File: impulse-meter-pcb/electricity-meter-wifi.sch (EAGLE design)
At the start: 13 parts, among them U2 MCP1316MT-29ME/OT

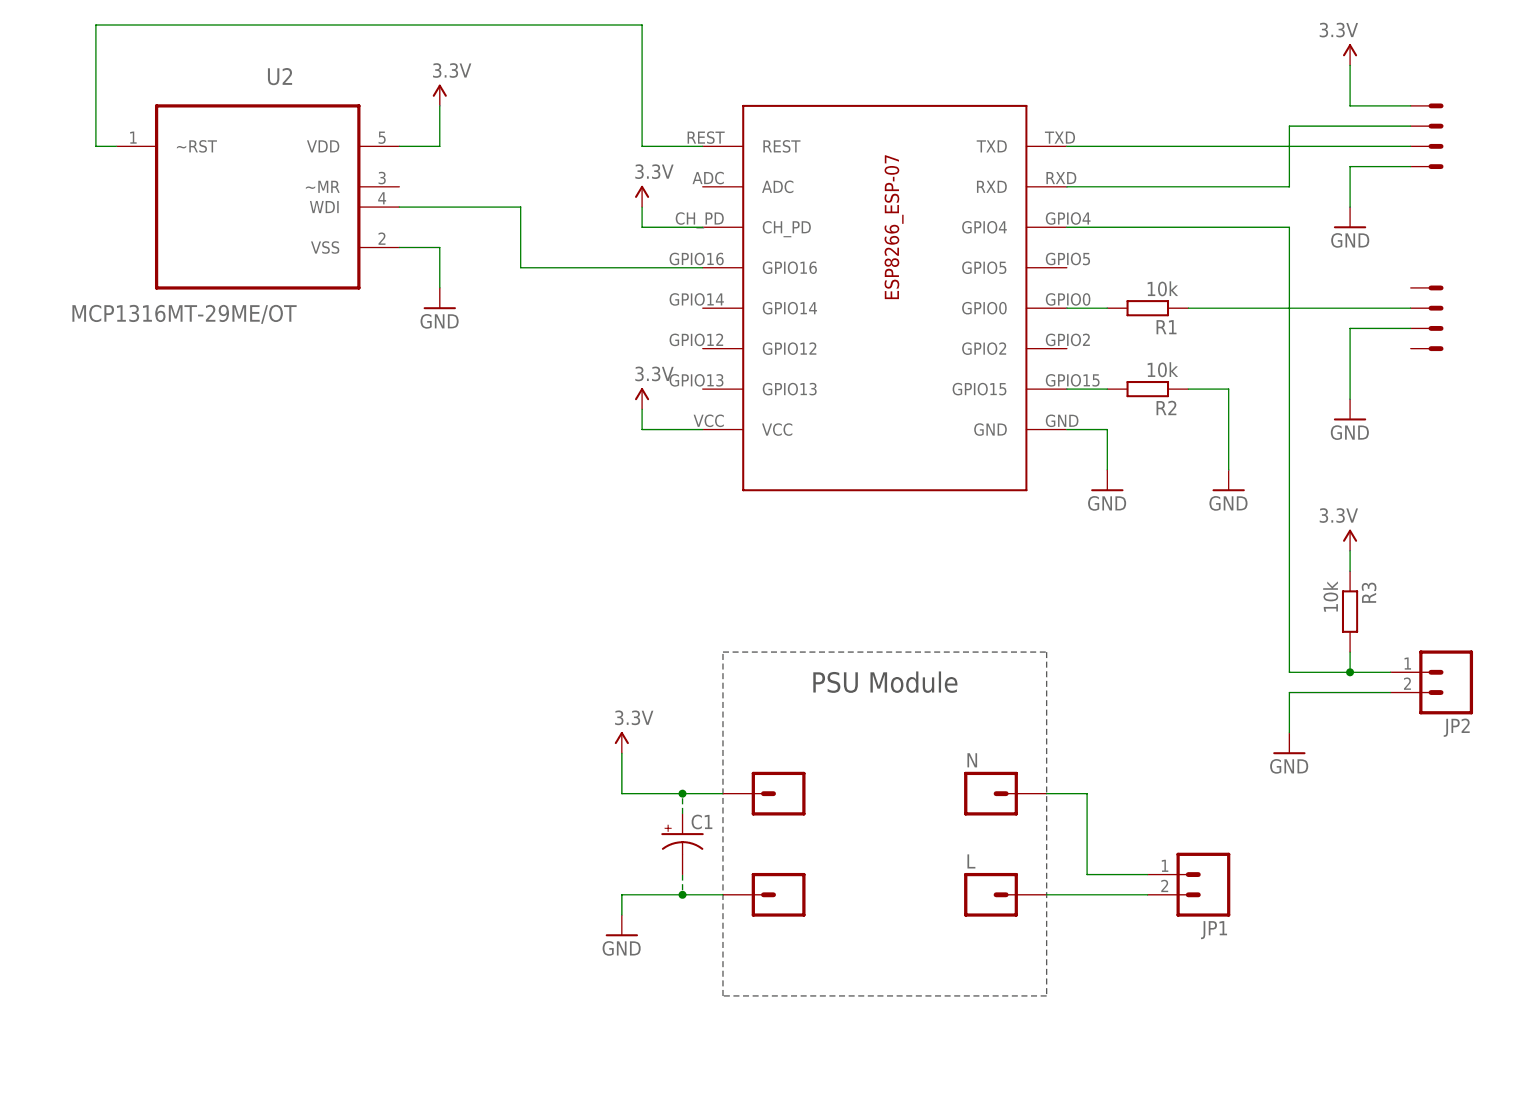
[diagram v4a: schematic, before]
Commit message: PCB: v.1.4.1 Added FeRAM
+ docs
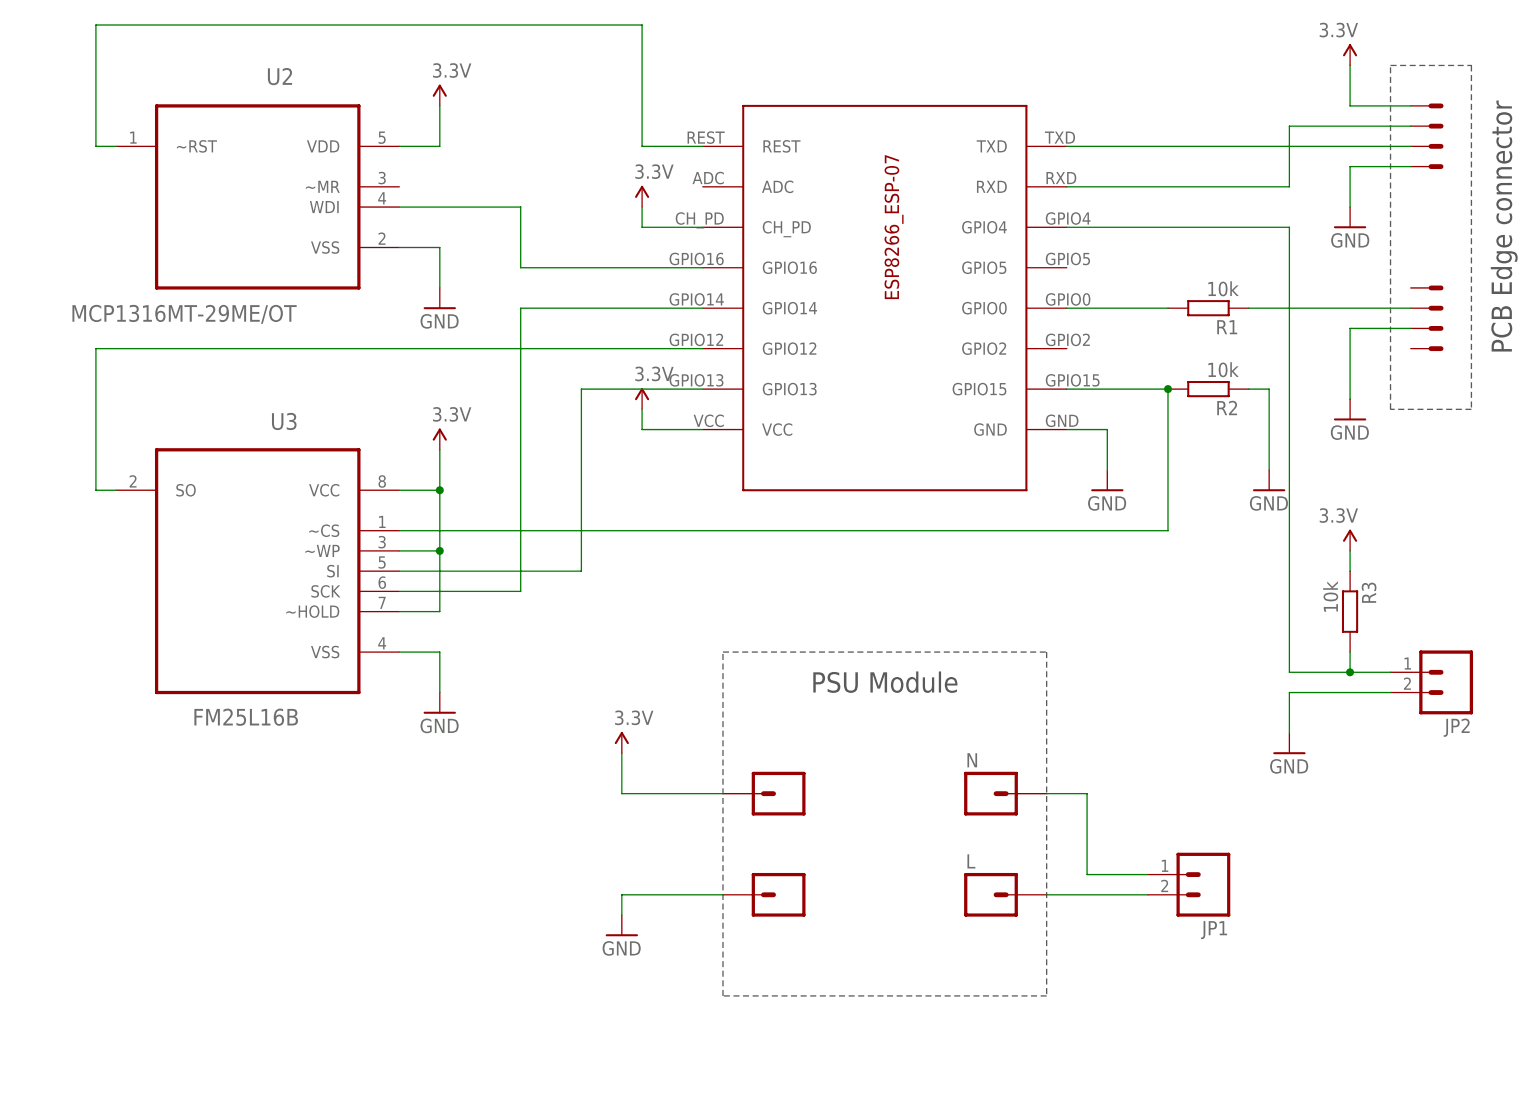
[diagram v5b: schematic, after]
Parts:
- removed C1: (no value), SparkFun-Capacitors:CAP_POLD
- added U3: FM25L16B, Microchip_By_element14_Batch_1:25AA020A-I/SN
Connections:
- new net N$10: ESP8266_ESP-07.GPIO12, U3.SO
- new net N$12: ESP8266_ESP-07.GPIO13, U3.SI
- new net N$13: ESP8266_ESP-07.GPIO14, U3.SCK
- net 3.3V: now also U3.VCC, U3.~HOLD, U3.~WP; no longer C1.+
- net GND: now also U3.VSS; no longer C1.-
- net N$7: now also U3.~CS
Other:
- note added: "PCB Edge connector"
- moved on the sheet: R1, R2
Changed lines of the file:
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@@
 <part name="JP1" library="SparkFun (old)" deviceset="M02" device="PTH3_5MM"/>
 <part name="JP2" library="SparkFun (old)" deviceset="M02" device="PTH3_5MM"/>
-<part name="C1" library="SparkFun-Capacitors" deviceset="CAP_POL" device="D"/>
 <part name="U$1" library="con-pcb-slot" deviceset="CON-PCB-SLOT-0.05" device="MINIMAL"/>
 <part name="GND2" library="SparkFun-Aesthetics" deviceset="GND" device=""/>
@@
 <part name="SUPPLY5" library="SparkFun-Aesthetics" deviceset="3.3V" device=""/>
 <part name="GND6" library="SparkFun-Aesthetics" deviceset="GND" device=""/>
+<part name="U3" library="Microchip_By_element14_Batch_1" deviceset="25AA020A-I/SN" device="" value="FM25L16B"/>
+<part name="GND7" library="SparkFun-Aesthetics" deviceset="GND" device=""/>
+<part name="SUPPLY6" library="SparkFun-Aesthetics" deviceset="3.3V" device=""/>
 </parts>
 <sheets>
@@
 <wire x1="129.54" y1="-27.94" x2="88.9" y2="-27.94" width="0.1524" layer="97" style="longdash"/>
 <text x="109.22" y="10.16" size="2.54" layer="97" align="bottom-center">PSU Module</text>
+<wire x1="172.72" y1="45.72" x2="172.72" y2="88.9" width="0.1524" layer="97" style="longdash"/>
+<wire x1="172.72" y1="88.9" x2="182.88" y2="88.9" width="0.1524" layer="97" style="longdash"/>
+<wire x1="182.88" y1="88.9" x2="182.88" y2="45.72" width="0.1524" layer="97" style="longdash"/>
+<wire x1="182.88" y1="45.72" x2="172.72" y2="45.72" width="0.1524" layer="97" style="longdash"/>
+<text x="187.96" y="68.58" size="2.54" layer="97" rot="R90" align="bottom-center">PCB Edge connector</text>
 </plain>
 <instances>
@@
 <instance part="SUPPLY4" gate="G$1" x="167.64" y="88.9" rot="MR0"/>
 <instance part="GND5" gate="1" x="167.64" y="44.45"/>
-<instance part="R1" gate="G$1" x="142.24" y="58.42" rot="R180"/>
+<instance part="R1" gate="G$1" x="149.86" y="58.42" rot="R180"/>
 <instance part="ESP8266_ESP-07" gate="G$1" x="106.68" y="53.34" smashed="yes">
 <attribute name="NAME" x="109.22" y="68.58" size="1.778" layer="94" rot="R270" align="bottom-center"/>
@@
 <instance part="JP1" gate="G$1" x="149.86" y="-12.7" rot="R180"/>
 <instance part="JP2" gate="G$1" x="180.34" y="12.7" rot="R180"/>
-<instance part="C1" gate="G$1" x="83.82" y="-7.62"/>
 <instance part="U$1" gate="G$1" x="175.26" y="76.2" smashed="yes" rot="MR180"/>
 <instance part="U$1" gate="G$2" x="175.26" y="78.74" smashed="yes" rot="MR180"/>
@@
 <instance part="R3" gate="G$1" x="167.64" y="20.32" rot="R270"/>
 <instance part="SUPPLY3" gate="G$1" x="167.64" y="27.94" rot="MR0"/>
-<instance part="R2" gate="G$1" x="142.24" y="48.26" rot="R180"/>
-<instance part="GND3" gate="1" x="152.4" y="35.56"/>
+<instance part="R2" gate="G$1" x="149.86" y="48.26" rot="R180"/>
+<instance part="GND3" gate="1" x="157.48" y="35.56"/>
 <instance part="U2" gate="A" x="30.48" y="76.2" rot="MR0"/>
 <instance part="SUPPLY5" gate="G$1" x="53.34" y="83.82"/>
 <instance part="GND6" gate="1" x="53.34" y="58.42"/>
+<instance part="U3" gate="A" x="30.48" y="27.94" rot="MR0"/>
+<instance part="GND7" gate="1" x="53.34" y="7.62"/>
+<instance part="SUPPLY6" gate="G$1" x="53.34" y="40.64"/>
 </instances>
 <busses>
@@
 <pinref part="GND" gate="G$1" pin="1"/>
 <pinref part="GND1" gate="1" pin="GND"/>
-<wire x1="88.9" y1="-15.24" x2="83.82" y2="-15.24" width="0.1524" layer="91"/>
-<wire x1="83.82" y1="-15.24" x2="76.2" y2="-15.24" width="0.1524" layer="91"/>
+<wire x1="88.9" y1="-15.24" x2="76.2" y2="-15.24" width="0.1524" layer="91"/>
 <wire x1="76.2" y1="-15.24" x2="76.2" y2="-17.78" width="0.1524" layer="91"/>
-<pinref part="C1" gate="G$1" pin="-"/>
-<wire x1="83.82" y1="-12.7" x2="83.82" y2="-15.24" width="0.1524" layer="91" style="longdash"/>
-<junction x="83.82" y="-15.24"/>
 </segment>
 <segment>
@@
 <segment>
 <pinref part="GND3" gate="1" pin="GND"/>
-<wire x1="152.4" y1="38.1" x2="152.4" y2="48.26" width="0.1524" layer="91"/>
+<wire x1="157.48" y1="38.1" x2="157.48" y2="48.26" width="0.1524" layer="91"/>
 <pinref part="R2" gate="G$1" pin="1"/>
-<wire x1="152.4" y1="48.26" x2="147.32" y2="48.26" width="0.1524" layer="91"/>
+<wire x1="157.48" y1="48.26" x2="154.94" y2="48.26" width="0.1524" layer="91"/>
 </segment>
 <segment>
@@
 <wire x1="53.34" y1="66.04" x2="53.34" y2="60.96" width="0.1524" layer="91"/>
 </segment>
+<segment>
+<pinref part="U3" gate="A" pin="VSS"/>
+<pinref part="GND7" gate="1" pin="GND"/>
+<wire x1="48.26" y1="15.24" x2="53.34" y2="15.24" width="0.1524" layer="91"/>
+<wire x1="53.34" y1="15.24" x2="53.34" y2="10.16" width="0.1524" layer="91"/>
+</segment>
 </net>
 <net name="3.3V" class="0">
@@
 <pinref part="3.3V" gate="G$1" pin="1"/>
 <pinref part="SUPPLY1" gate="G$1" pin="3.3V"/>
-<wire x1="88.9" y1="-2.54" x2="83.82" y2="-2.54" width="0.1524" layer="91"/>
-<wire x1="83.82" y1="-2.54" x2="76.2" y2="-2.54" width="0.1524" layer="91"/>
+<wire x1="88.9" y1="-2.54" x2="76.2" y2="-2.54" width="0.1524" layer="91"/>
 <wire x1="76.2" y1="-2.54" x2="76.2" y2="2.54" width="0.1524" layer="91"/>
-<pinref part="C1" gate="G$1" pin="+"/>
-<wire x1="83.82" y1="-5.08" x2="83.82" y2="-2.54" width="0.1524" layer="91" style="longdash"/>
-<junction x="83.82" y="-2.54"/>
 </segment>
 <segment>
@@
 <wire x1="53.34" y1="78.74" x2="53.34" y2="83.82" width="0.1524" layer="91"/>
 </segment>
+<segment>
+<pinref part="U3" gate="A" pin="VCC"/>
+<pinref part="SUPPLY6" gate="G$1" pin="3.3V"/>
+<wire x1="48.26" y1="35.56" x2="53.34" y2="35.56" width="0.1524" layer="91"/>
+<wire x1="53.34" y1="35.56" x2="53.34" y2="40.64" width="0.1524" layer="91"/>
+<pinref part="U3" gate="A" pin="~WP"/>
+<wire x1="48.26" y1="27.94" x2="53.34" y2="27.94" width="0.1524" layer="91"/>
+<wire x1="53.34" y1="27.94" x2="53.34" y2="35.56" width="0.1524" layer="91"/>
+<junction x="53.34" y="35.56"/>
+<pinref part="U3" gate="A" pin="~HOLD"/>
+<wire x1="48.26" y1="20.32" x2="53.34" y2="20.32" width="0.1524" layer="91"/>
+<wire x1="53.34" y1="20.32" x2="53.34" y2="27.94" width="0.1524" layer="91"/>
+<junction x="53.34" y="27.94"/>
+</segment>
 </net>
 <net name="N$11" class="0">
@@
 <pinref part="R1" gate="G$1" pin="1"/>
 <pinref part="U$1" gate="G$6" pin="S"/>
-<wire x1="147.32" y1="58.42" x2="175.26" y2="58.42" width="0.1524" layer="91"/>
+<wire x1="154.94" y1="58.42" x2="175.26" y2="58.42" width="0.1524" layer="91"/>
 </segment>
 </net>
@@
 <pinref part="R1" gate="G$1" pin="2"/>
 <pinref part="ESP8266_ESP-07" gate="G$1" pin="GPIO0"/>
-<wire x1="137.16" y1="58.42" x2="132.08" y2="58.42" width="0.1524" layer="91"/>
+<wire x1="144.78" y1="58.42" x2="132.08" y2="58.42" width="0.1524" layer="91"/>
 </segment>
 </net>
@@
 <pinref part="R2" gate="G$1" pin="2"/>
 <pinref part="ESP8266_ESP-07" gate="G$1" pin="GPIO15"/>
-<wire x1="137.16" y1="48.26" x2="132.08" y2="48.26" width="0.1524" layer="91"/>
+<wire x1="144.78" y1="48.26" x2="132.08" y2="48.26" width="0.1524" layer="91"/>
+<pinref part="U3" gate="A" pin="~CS"/>
+<wire x1="48.26" y1="30.48" x2="144.78" y2="30.48" width="0.1524" layer="91"/>
+<wire x1="144.78" y1="30.48" x2="144.78" y2="48.26" width="0.1524" layer="91"/>
+<junction x="144.78" y="48.26"/>
 </segment>
 </net>
@@
 </segment>
 </net>
+<net name="N$10" class="0">
+<segment>
+<pinref part="U3" gate="A" pin="SO"/>
+<wire x1="12.7" y1="35.56" x2="10.16" y2="35.56" width="0.1524" layer="91"/>
+<wire x1="10.16" y1="35.56" x2="10.16" y2="53.34" width="0.1524" layer="91"/>
+<pinref part="ESP8266_ESP-07" gate="G$1" pin="GPIO12"/>
+<wire x1="10.16" y1="53.34" x2="86.36" y2="53.34" width="0.1524" layer="91"/>
+</segment>
+</net>
+<net name="N$12" class="0">
+<segment>
+<pinref part="U3" gate="A" pin="SI"/>
+<wire x1="48.26" y1="25.4" x2="71.12" y2="25.4" width="0.1524" layer="91"/>
+<wire x1="71.12" y1="25.4" x2="71.12" y2="48.26" width="0.1524" layer="91"/>
+<pinref part="ESP8266_ESP-07" gate="G$1" pin="GPIO13"/>
+<wire x1="71.12" y1="48.26" x2="86.36" y2="48.26" width="0.1524" layer="91"/>
+</segment>
+</net>
+<net name="N$13" class="0">
+<segment>
+<pinref part="U3" gate="A" pin="SCK"/>
+<wire x1="48.26" y1="22.86" x2="63.5" y2="22.86" width="0.1524" layer="91"/>
+<wire x1="63.5" y1="22.86" x2="63.5" y2="58.42" width="0.1524" layer="91"/>
+<pinref part="ESP8266_ESP-07" gate="G$1" pin="GPIO14"/>
+<wire x1="63.5" y1="58.42" x2="86.36" y2="58.42" width="0.1524" layer="91"/>
+</segment>
+</net>

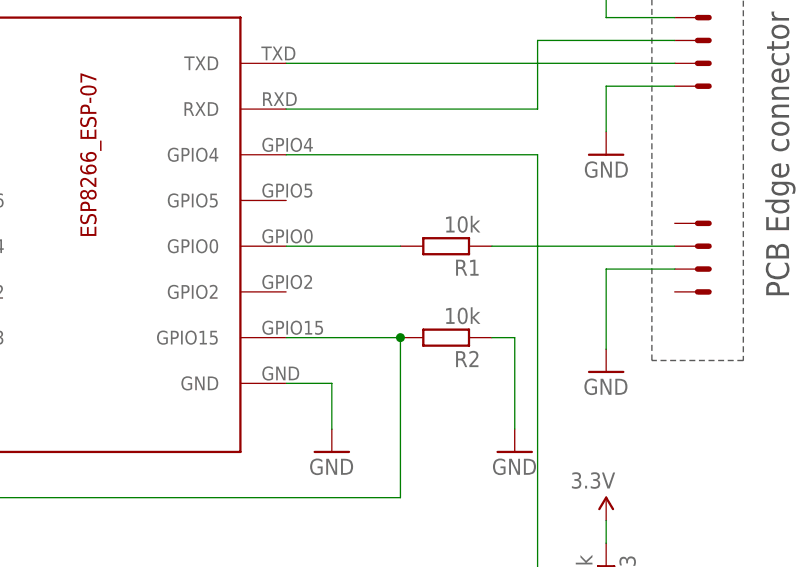
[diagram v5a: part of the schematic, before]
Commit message: added pull up resistor on GPIO02
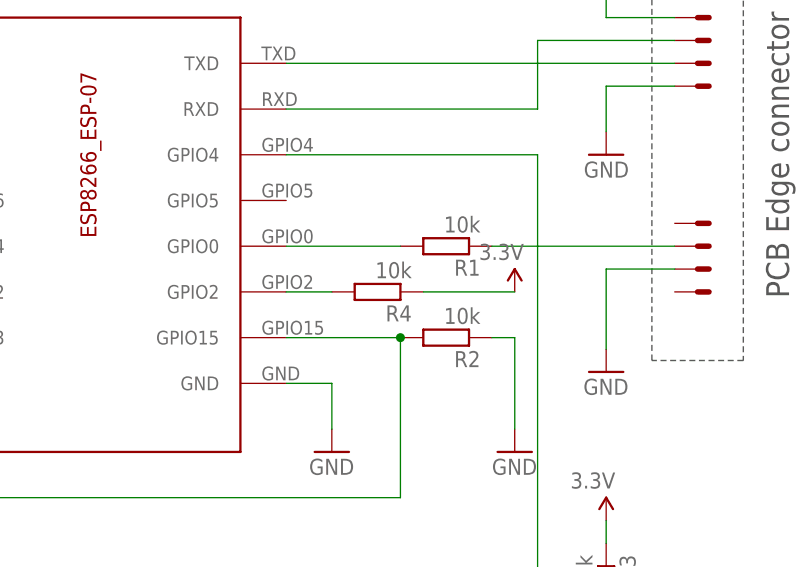
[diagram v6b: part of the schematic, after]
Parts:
- added R4: 10k, rcl:R-EU_R0805
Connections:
- new net N$14: ESP8266_ESP-07.GPIO2, R4.2
- net 3.3V: now also R4.1
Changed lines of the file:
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@@
 <?xml version="1.0" encoding="utf-8"?>
 <!DOCTYPE eagle SYSTEM "eagle.dtd">
-<eagle version="7.2.0">
+<eagle version="7.6.0">
 <drawing>
 <settings>
@@
 <part name="GND7" library="SparkFun-Aesthetics" deviceset="GND" device=""/>
 <part name="SUPPLY6" library="SparkFun-Aesthetics" deviceset="3.3V" device=""/>
+<part name="SUPPLY8" library="SparkFun-Aesthetics" deviceset="3.3V" device=""/>
+<part name="R4" library="rcl" deviceset="R-EU_" device="R0805" value="10k"/>
 </parts>
 <sheets>
@@
 <instance part="GND7" gate="1" x="53.34" y="7.62"/>
 <instance part="SUPPLY6" gate="G$1" x="53.34" y="40.64"/>
+<instance part="SUPPLY8" gate="G$1" x="157.48" y="53.34" rot="MR0"/>
+<instance part="R4" gate="G$1" x="142.24" y="53.34" rot="R180"/>
 </instances>
 <busses>
@@
 <junction x="53.34" y="27.94"/>
 </segment>
+<segment>
+<pinref part="R4" gate="G$1" pin="1"/>
+<pinref part="SUPPLY8" gate="G$1" pin="3.3V"/>
+<wire x1="147.32" y1="53.34" x2="157.48" y2="53.34" width="0.1524" layer="91"/>
+</segment>
 </net>
 <net name="N$11" class="0">
@@
 </segment>
 </net>
+<net name="N$14" class="0">
+<segment>
+<pinref part="ESP8266_ESP-07" gate="G$1" pin="GPIO2"/>
+<pinref part="R4" gate="G$1" pin="2"/>
+<wire x1="132.08" y1="53.34" x2="137.16" y2="53.34" width="0.1524" layer="91"/>
+</segment>
+</net>
